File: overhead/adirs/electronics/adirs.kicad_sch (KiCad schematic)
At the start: 3 parts

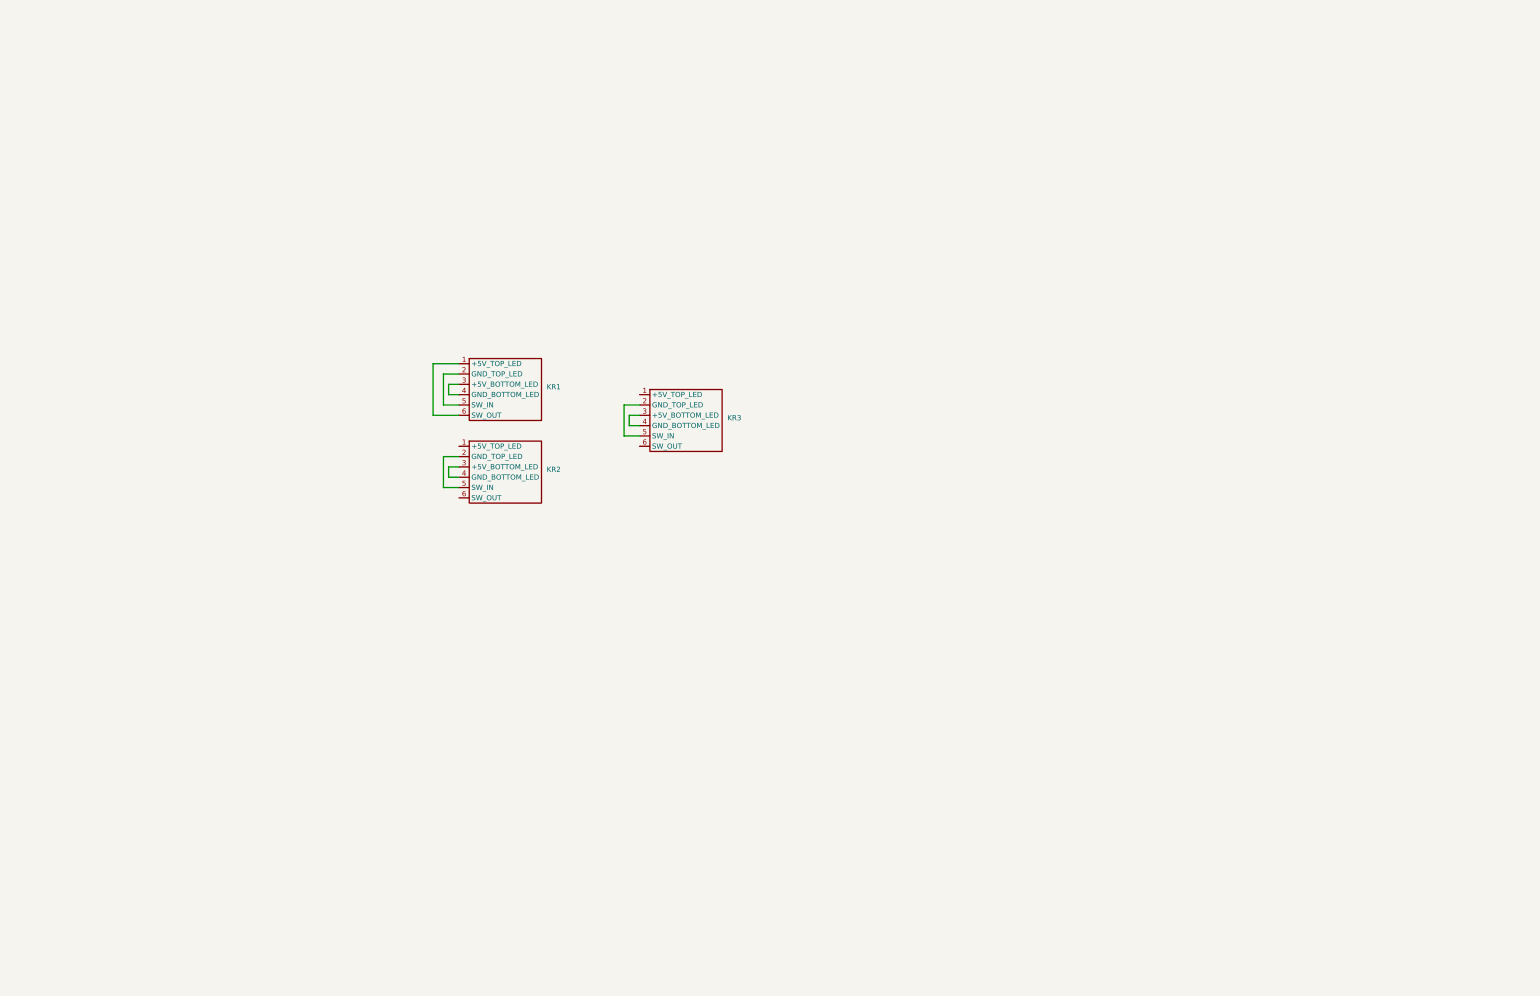
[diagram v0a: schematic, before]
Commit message: Started work for ADIRS Schematic and PCB
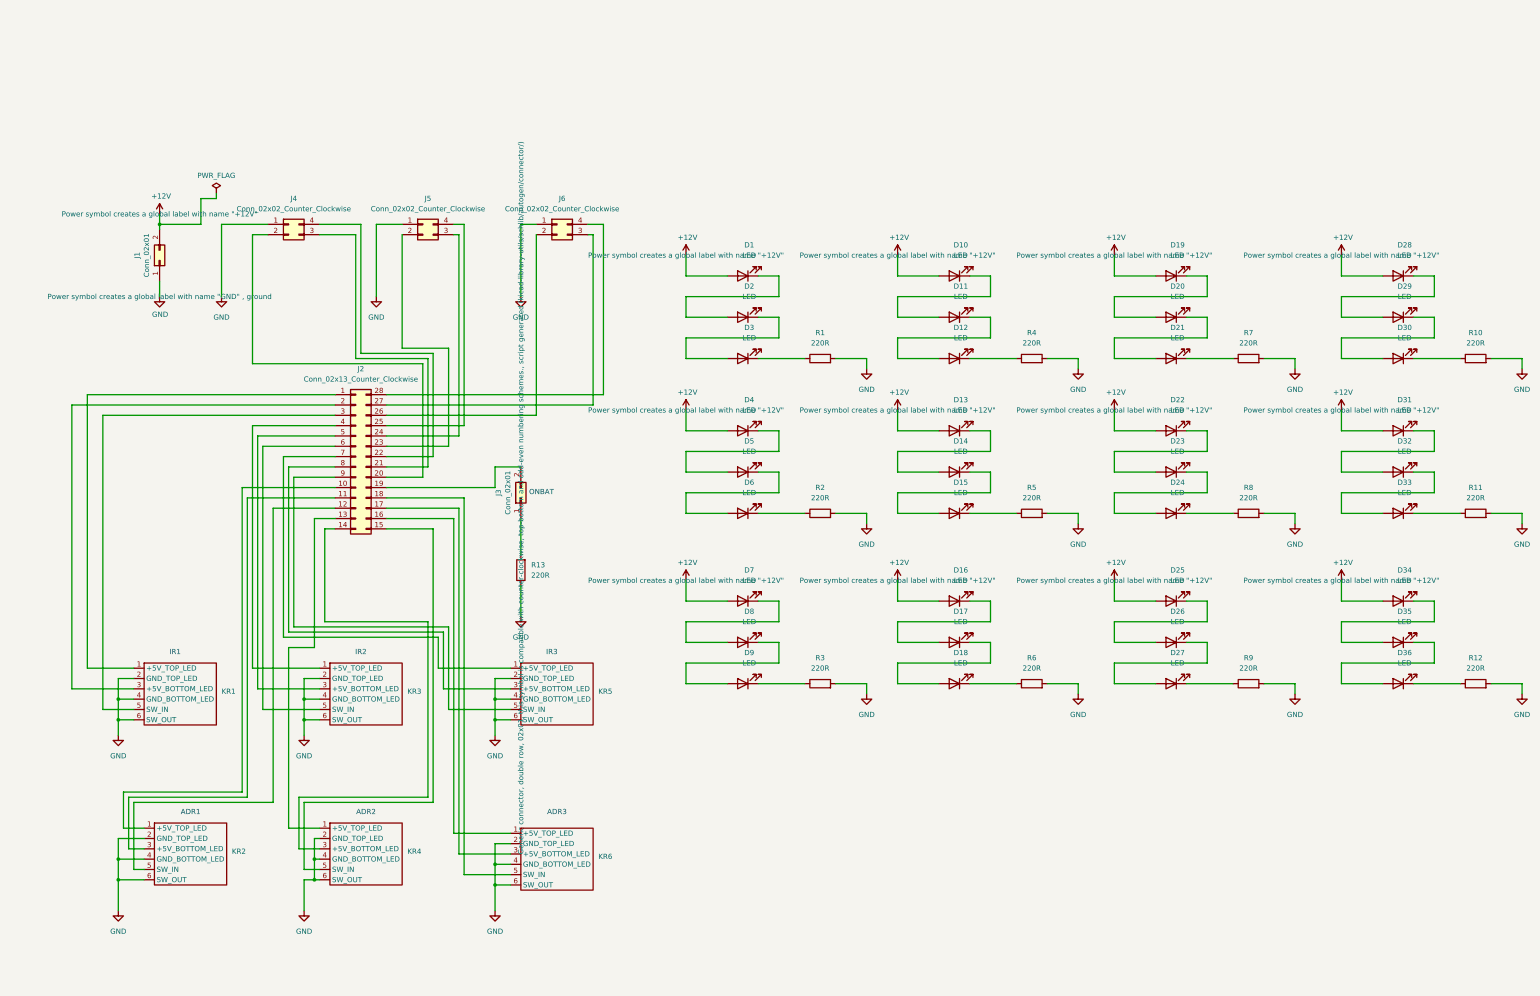
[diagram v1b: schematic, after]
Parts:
- added D1, D10, D11, D12, D13, D14, D15, D16, D17, D18, D19, D2, D20, D21, D22, D23, D24, D25, D26, D27, D28, D29, D3, D30, D31, D32, D33, D34, D35, D36, D4, D5, D6, D7, D8, D9: LED, LED_THT:LED_D5.0mm, symbol Device:LED
- added J1, J3: Conn_02x01, TerminalBlock:TerminalBlock_bornier-2_P5.08mm, symbol Connector_Generic:Conn_02x01
- added J2: Conn_02x13_Counter_Clockwise, TerminalBlock:TerminalBlock_bornier-2_P5.08mm, symbol Connector_Generic:Conn_02x14_Counter_Clockwise
- added J4, J5, J6: Conn_02x02_Counter_Clockwise, TerminalBlock:TerminalBlock_bornier-2_P5.08mm, symbol Connector_Generic:Conn_02x02_Counter_Clockwise
- added KR4, KR5, KR6: ~, KorrySwitch:OpenA3XX, symbol KorrySwitch:Korry_Switch
- added R1, R10, R11, R12, R13, R2, R3, R4, R5, R6, R7, R8, R9: 220R, Resistor_SMD:R_1206_3216Metric_Pad1.30x1.75mm_HandSolder, symbol Device:R
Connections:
- net at KR1.1 (+5V_TOP_LED): now also J2.1 (Pin_1); no longer KR1.6 (SW_OUT)
- net at KR1.5 (SW_IN): now also J2.3 (Pin_3); no longer KR1.2 (GND_TOP_LED)
- net at KR1.3 (+5V_BOTTOM_LED): now also J2.2 (Pin_2); no longer KR1.4 (GND_BOTTOM_LED)
- net at KR3.1 (+5V_TOP_LED): now also J2.4 (Pin_4)
- net at KR3.5 (SW_IN): now also J2.6 (Pin_6); no longer KR3.2 (GND_TOP_LED)
- net at KR3.3 (+5V_BOTTOM_LED): now also J2.5 (Pin_5); no longer KR3.4 (GND_BOTTOM_LED)
- net GND: now reaches KR3.6 (SW_OUT)
- net GND: now also KR1.2 (GND_TOP_LED), KR1.4 (GND_BOTTOM_LED), KR1.6 (SW_OUT), KR2.2 (GND_TOP_LED), KR2.4 (GND_BOTTOM_LED), KR2.6 (SW_OUT), KR3.2 (GND_TOP_LED), KR3.4 (GND_BOTTOM_LED), J1.1 (Pin_1), J4.1 (Pin_1), J5.1 (Pin_1), J6.1 (Pin_1), KR4.2 (GND_TOP_LED), KR4.4 (GND_BOTTOM_LED), KR4.6 (SW_OUT), KR5.2 (GND_TOP_LED), KR5.4 (GND_BOTTOM_LED), KR5.6 (SW_OUT), KR6.2 (GND_TOP_LED), KR6.4 (GND_BOTTOM_LED), KR6.6 (SW_OUT), R1.2, R10.2, R11.2, R12.2, R13.1, R2.2, R3.2, R4.2, R5.2, R6.2, R7.2, R8.2, R9.2
- net at KR2.1 (+5V_TOP_LED): now also J2.10 (Pin_10)
- net at KR2.5 (SW_IN): now also J2.12 (Pin_12); no longer KR2.2 (GND_TOP_LED)
- net at KR2.3 (+5V_BOTTOM_LED): now also J2.11 (Pin_11); no longer KR2.4 (GND_BOTTOM_LED)
- new net: D27.1 (K), R9.1
- new net: J2.20 (Pin_20), J4.2 (Pin_2)
- new net: J2.21 (Pin_21), J4.3 (Pin_3)
- new net: J2.22 (Pin_22), J4.4 (Pin_4)
- new net: D17.1 (K), D18.2 (A)
- new net: D16.1 (K), D17.2 (A)
- new net: D5.1 (K), D6.2 (A)
- new net: D4.1 (K), D5.2 (A)
- new net: D30.1 (K), R10.1
- new net: D29.1 (K), D30.2 (A)
- new net: D6.1 (K), R2.1
- new net: D20.1 (K), D21.2 (A)
- new net: D19.1 (K), D20.2 (A)
- new net: D3.1 (K), R1.1
- new net: D28.1 (K), D29.2 (A)
- new net: D33.1 (K), R11.1
- new net: D26.1 (K), D27.2 (A)
- new net: D25.1 (K), D26.2 (A)
- new net: J3.1 (Pin_1), R13.2
- new net: J2.13 (Pin_13), KR4.1 (+5V_TOP_LED)
- new net: J2.14 (Pin_14), KR4.3 (+5V_BOTTOM_LED)
- new net: J2.15 (Pin_15), KR4.5 (SW_IN)
- new net: J2.19 (Pin_19), J3.2 (Pin_2)
- new net: D8.1 (K), D9.2 (A)
- new net: D7.1 (K), D8.2 (A)
- new net: D24.1 (K), R8.1
- new net: D23.1 (K), D24.2 (A)
- new net: D21.1 (K), R7.1
- new net: D10.1 (K), D11.2 (A)
- new net: J2.26 (Pin_26), J6.2 (Pin_2)
- new net: J2.27 (Pin_27), J6.3 (Pin_3)
- new net: J2.28 (Pin_28), J6.4 (Pin_4)
- new net: D22.1 (K), D23.2 (A)
- new net: D32.1 (K), D33.2 (A)
- new net: D12.1 (K), R4.1
- new net: D11.1 (K), D12.2 (A)
- new net: J2.16 (Pin_16), KR6.1 (+5V_TOP_LED)
- new net: J2.17 (Pin_17), KR6.3 (+5V_BOTTOM_LED)
- new net: J2.18 (Pin_18), KR6.5 (SW_IN)
- new net: J2.23 (Pin_23), J5.2 (Pin_2)
- new net: J2.24 (Pin_24), J5.3 (Pin_3)
- new net: J2.25 (Pin_25), J5.4 (Pin_4)
- new net: J2.7 (Pin_7), KR5.1 (+5V_TOP_LED)
- new net: J2.8 (Pin_8), KR5.3 (+5V_BOTTOM_LED)
- new net: J2.9 (Pin_9), KR5.5 (SW_IN)
- new net: D9.1 (K), R3.1
- new net: D31.1 (K), D32.2 (A)
- new net: D34.1 (K), D35.2 (A)
- new net: D15.1 (K), R5.1
- new net: D1.1 (K), D2.2 (A)
- new net: D2.1 (K), D3.2 (A)
- new net: D14.1 (K), D15.2 (A)
- new net: D13.1 (K), D14.2 (A)
- new net: D18.1 (K), R6.1
- new net: D36.1 (K), R12.1
- new net: D35.1 (K), D36.2 (A)
- new net +12V: D1.2 (A), D10.2 (A), D13.2 (A), D16.2 (A), D19.2 (A), D22.2 (A), D25.2 (A), D28.2 (A), D31.2 (A), D34.2 (A), D4.2 (A), D7.2 (A), J1.2 (Pin_2)
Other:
- note added: "ADR1"
- note added: "ADR2"
- note added: "ADR3"
- note added: "IR1"
- note added: "IR2"
- note added: "IR3"
- note added: "ONBAT"

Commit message: Updates and Routing to ADIRS PCB and Schematic
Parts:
- added D37, D38, D39, D40: LED, LED_THT:LED_D5.0mm, symbol Device:LED
- added R14, R15: 220R, Resistor_SMD:R_1206_3216Metric_Pad1.30x1.75mm_HandSolder, symbol Device:R
- J2: footprint TerminalBlock:TerminalBlock_bornier-2_P5.08mm -> Connector_PinHeader_2.54mm:PinHeader_2x14_P2.54mm_Vertical
- J3: footprint TerminalBlock:TerminalBlock_bornier-2_P5.08mm -> Connector_PinHeader_2.54mm:PinHeader_1x02_P2.54mm_Vertical
- J4, J5, J6: footprint TerminalBlock:TerminalBlock_bornier-2_P5.08mm -> TerminalBlock:TerminalBlock_bornier-4_P5.08mm
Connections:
- net +12V: now also D37.2 (A), D40.2 (A)
- net GND: now also R14.2, R15.2
- new net: D39.1 (K), R14.1
- new net: D40.1 (K), R15.1
- new net: D38.1 (K), D39.2 (A)
- new net: D37.1 (K), D38.2 (A)

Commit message: Improvements to ADIRS - and setting up PCB design Baseline
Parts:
- D1, D10, D11, D12, D13, D14, D15, D16, D17, D18, D19, D2, D20, D21, D22, D23, D24, D25, D26, D27, D28, D29, D3, D30, D31, D32, D33, D34, D35, D36, D37, D38, D39, D4, D40, D5, D6, D7, D8, D9: footprint LED_THT:LED_D5.0mm -> LED_THT:LED_D5.0mm_Clear
- J4, J5, J6: footprint TerminalBlock:TerminalBlock_bornier-4_P5.08mm -> Connector_PinHeader_2.54mm:PinHeader_1x04_P2.54mm_Vertical
- KR1, KR2, KR3, KR4, KR5, KR6: footprint KorrySwitch:OpenA3XX -> OpenA3XX:Korry Switch
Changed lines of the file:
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@@
 			)
 		)
-		(property "Footprint" "TerminalBlock:TerminalBlock_bornier-4_P5.08mm"
+		(property "Footprint" "Connector_PinHeader_2.54mm:PinHeader_1x04_P2.54mm_Vertical"
 			(at 77.47 33.02 0)
 			(effects
@@
 			)
 		)
-		(property "Footprint" "LED_THT:LED_D5.0mm"
+		(property "Footprint" "LED_THT:LED_D5.0mm_Clear"
 			(at 241.3 135.89 0)
 			(effects
@@
 			)
 		)
-		(property "Footprint" "LED_THT:LED_D5.0mm"
+		(property "Footprint" "LED_THT:LED_D5.0mm_Clear"
 			(at 189.23 93.98 0)
 			(effects
@@
 			)
 		)
-		(property "Footprint" "LED_THT:LED_D5.0mm"
+		(property "Footprint" "LED_THT:LED_D5.0mm_Clear"
 			(at 350.52 66.04 0)
 			(effects
@@
 			)
 		)
-		(property "Footprint" "LED_THT:LED_D5.0mm"
+		(property "Footprint" "LED_THT:LED_D5.0mm_Clear"
 			(at 189.23 104.14 0)
 			(effects
@@
 			)
 		)
-		(property "Footprint" "LED_THT:LED_D5.0mm"
+		(property "Footprint" "LED_THT:LED_D5.0mm_Clear"
 			(at 294.64 55.88 0)
 			(effects
@@
 			)
 		)
-		(property "Footprint" "LED_THT:LED_D5.0mm"
+		(property "Footprint" "LED_THT:LED_D5.0mm_Clear"
 			(at 350.52 55.88 0)
 			(effects
@@
 			)
 		)
-		(property "Footprint" "LED_THT:LED_D5.0mm"
+		(property "Footprint" "LED_THT:LED_D5.0mm_Clear"
 			(at 294.64 135.89 0)
 			(effects
@@
 			)
 		)
-		(property "Footprint" "KorrySwitch:OpenA3XX"
+		(property "Footprint" "OpenA3XX:Korry Switch"
 			(at 95.25 177.8 0)
 			(effects
@@
 			)
 		)
-		(property "Footprint" "LED_THT:LED_D5.0mm"
+		(property "Footprint" "LED_THT:LED_D5.0mm_Clear"
 			(at 242.57 170.18 0)
 			(effects
@@
 			)
 		)
-		(property "Footprint" "LED_THT:LED_D5.0mm"
+		(property "Footprint" "LED_THT:LED_D5.0mm_Clear"
 			(at 189.23 135.89 0)
 			(effects
@@
 			)
 		)
-		(property "Footprint" "LED_THT:LED_D5.0mm"
+		(property "Footprint" "LED_THT:LED_D5.0mm_Clear"
 			(at 294.64 104.14 0)
 			(effects
@@
 			)
 		)
-		(property "Footprint" "LED_THT:LED_D5.0mm"
+		(property "Footprint" "LED_THT:LED_D5.0mm_Clear"
 			(at 294.64 66.04 0)
 			(effects
@@
 			)
 		)
-		(property "Footprint" "LED_THT:LED_D5.0mm"
+		(property "Footprint" "LED_THT:LED_D5.0mm_Clear"
 			(at 241.3 45.72 0)
 			(effects
@@
 			)
 		)
-		(property "Footprint" "TerminalBlock:TerminalBlock_bornier-4_P5.08mm"
+		(property "Footprint" "Connector_PinHeader_2.54mm:PinHeader_1x04_P2.54mm_Vertical"
 			(at 143.51 33.02 0)
 			(effects
@@
 			)
 		)
-		(property "Footprint" "LED_THT:LED_D5.0mm"
+		(property "Footprint" "LED_THT:LED_D5.0mm_Clear"
 			(at 294.64 83.82 0)
 			(effects
@@
 			)
 		)
-		(property "Footprint" "LED_THT:LED_D5.0mm"
+		(property "Footprint" "LED_THT:LED_D5.0mm_Clear"
 			(at 294.64 146.05 0)
 			(effects
@@
 			)
 		)
-		(property "Footprint" "LED_THT:LED_D5.0mm"
+		(property "Footprint" "LED_THT:LED_D5.0mm_Clear"
 			(at 350.52 104.14 0)
 			(effects
@@
 			)
 		)
-		(property "Footprint" "LED_THT:LED_D5.0mm"
+		(property "Footprint" "LED_THT:LED_D5.0mm_Clear"
 			(at 241.3 66.04 0)
 			(effects
@@
 			)
 		)
-		(property "Footprint" "LED_THT:LED_D5.0mm"
+		(property "Footprint" "LED_THT:LED_D5.0mm_Clear"
 			(at 350.52 45.72 0)
 			(effects
@@
 			)
 		)
-		(property "Footprint" "LED_THT:LED_D5.0mm"
+		(property "Footprint" "LED_THT:LED_D5.0mm_Clear"
 			(at 350.52 83.82 0)
 			(effects
@@
 			)
 		)
-		(property "Footprint" "LED_THT:LED_D5.0mm"
+		(property "Footprint" "LED_THT:LED_D5.0mm_Clear"
 			(at 189.23 189.23 0)
 			(effects
@@
 			)
 		)
-		(property "Footprint" "LED_THT:LED_D5.0mm"
+		(property "Footprint" "LED_THT:LED_D5.0mm_Clear"
 			(at 189.23 146.05 0)
 			(effects
@@
 			)
 		)
-		(property "Footprint" "LED_THT:LED_D5.0mm"
+		(property "Footprint" "LED_THT:LED_D5.0mm_Clear"
 			(at 350.52 125.73 0)
 			(effects
@@
 			)
 		)
-		(property "Footprint" "LED_THT:LED_D5.0mm"
+		(property "Footprint" "LED_THT:LED_D5.0mm_Clear"
 			(at 294.64 45.72 0)
 			(effects
@@
 			)
 		)
-		(property "Footprint" "LED_THT:LED_D5.0mm"
+		(property "Footprint" "LED_THT:LED_D5.0mm_Clear"
 			(at 294.64 93.98 0)
 			(effects
@@
 			)
 		)
-		(property "Footprint" "LED_THT:LED_D5.0mm"
+		(property "Footprint" "LED_THT:LED_D5.0mm_Clear"
 			(at 241.3 125.73 0)
 			(effects
@@
 			)
 		)
-		(property "Footprint" "LED_THT:LED_D5.0mm"
+		(property "Footprint" "LED_THT:LED_D5.0mm_Clear"
 			(at 189.23 45.72 0)
 			(effects
@@
 			)
 		)
-		(property "Footprint" "LED_THT:LED_D5.0mm"
+		(property "Footprint" "LED_THT:LED_D5.0mm_Clear"
 			(at 189.23 55.88 0)
 			(effects
@@
 			)
 		)
-		(property "Footprint" "KorrySwitch:OpenA3XX"
+		(property "Footprint" "OpenA3XX:Korry Switch"
 			(at 142.24 179.07 0)
 			(effects
@@
 			)
 		)
-		(property "Footprint" "KorrySwitch:OpenA3XX"
+		(property "Footprint" "OpenA3XX:Korry Switch"
 			(at 95.25 138.43 0)
 			(effects
@@
 			)
 		)
-		(property "Footprint" "TerminalBlock:TerminalBlock_bornier-4_P5.08mm"
+		(property "Footprint" "Connector_PinHeader_2.54mm:PinHeader_1x04_P2.54mm_Vertical"
 			(at 110.49 33.02 0)
 			(effects
@@
 			)
 		)
-		(property "Footprint" "LED_THT:LED_D5.0mm"
+		(property "Footprint" "LED_THT:LED_D5.0mm_Clear"
 			(at 189.23 83.82 0)
 			(effects
@@
 			)
 		)
-		(property "Footprint" "LED_THT:LED_D5.0mm"
+		(property "Footprint" "LED_THT:LED_D5.0mm_Clear"
 			(at 241.3 93.98 0)
 			(effects
@@
 			)
 		)
-		(property "Footprint" "LED_THT:LED_D5.0mm"
+		(property "Footprint" "LED_THT:LED_D5.0mm_Clear"
 			(at 241.3 104.14 0)
 			(effects
@@
 			)
 		)
-		(property "Footprint" "LED_THT:LED_D5.0mm"
+		(property "Footprint" "LED_THT:LED_D5.0mm_Clear"
 			(at 189.23 168.91 0)
 			(effects
@@
 			)
 		)
-		(property "Footprint" "LED_THT:LED_D5.0mm"
+		(property "Footprint" "LED_THT:LED_D5.0mm_Clear"
 			(at 241.3 83.82 0)
 			(effects
@@
 			)
 		)
-		(property "Footprint" "LED_THT:LED_D5.0mm"
+		(property "Footprint" "LED_THT:LED_D5.0mm_Clear"
 			(at 350.52 146.05 0)
 			(effects
@@
 			)
 		)
-		(property "Footprint" "KorrySwitch:OpenA3XX"
+		(property "Footprint" "OpenA3XX:Korry Switch"
 			(at 52.07 177.8 0)
 			(effects
@@
 			)
 		)
-		(property "Footprint" "LED_THT:LED_D5.0mm"
+		(property "Footprint" "LED_THT:LED_D5.0mm_Clear"
 			(at 189.23 179.07 0)
 			(effects
@@
 			)
 		)
-		(property "Footprint" "KorrySwitch:OpenA3XX"
+		(property "Footprint" "OpenA3XX:Korry Switch"
 			(at 49.53 138.43 0)
 			(effects
@@
 			)
 		)
-		(property "Footprint" "KorrySwitch:OpenA3XX"
+		(property "Footprint" "OpenA3XX:Korry Switch"
 			(at 142.24 138.43 0)
 			(effects
@@
 			)
 		)
-		(property "Footprint" "LED_THT:LED_D5.0mm"
+		(property "Footprint" "LED_THT:LED_D5.0mm_Clear"
 			(at 189.23 125.73 0)
 			(effects
@@
 			)
 		)
-		(property "Footprint" "LED_THT:LED_D5.0mm"
+		(property "Footprint" "LED_THT:LED_D5.0mm_Clear"
 			(at 241.3 146.05 0)
 			(effects
@@
 			)
 		)
-		(property "Footprint" "LED_THT:LED_D5.0mm"
+		(property "Footprint" "LED_THT:LED_D5.0mm_Clear"
 			(at 189.23 66.04 0)
 			(effects
@@
 			)
 		)
-		(property "Footprint" "LED_THT:LED_D5.0mm"
+		(property "Footprint" "LED_THT:LED_D5.0mm_Clear"
 			(at 350.52 135.89 0)
 			(effects
@@
 			)
 		)
-		(property "Footprint" "LED_THT:LED_D5.0mm"
+		(property "Footprint" "LED_THT:LED_D5.0mm_Clear"
 			(at 294.64 125.73 0)
 			(effects
@@
 			)
 		)
-		(property "Footprint" "LED_THT:LED_D5.0mm"
+		(property "Footprint" "LED_THT:LED_D5.0mm_Clear"
 			(at 350.52 93.98 0)
 			(effects
@@
 			)
 		)
-		(property "Footprint" "LED_THT:LED_D5.0mm"
+		(property "Footprint" "LED_THT:LED_D5.0mm_Clear"
 			(at 241.3 55.88 0)
 			(effects
